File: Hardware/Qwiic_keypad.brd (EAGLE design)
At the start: 31.8 x 25.4 mm, 25 parts, among them J2 SMD, J3 PTH, J4 SMD, J6 AVR_SPI_PROG_3X2TESTPOINTS, U3 ATTINY84

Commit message: second layout complete
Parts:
- moved R3 6.48 mm to (14.0, 6.35)
- moved C4 5.24 mm to (7.62, 6.35)
- moved JP3 2.84 mm to (3.81, 1.27)
- moved JP5 1.27 mm to (17.8, 6.35)
- moved R1 1.27 mm to (24.1, 6.35)
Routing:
- net 3.3V: track 0.00 -> 77.5 mm, vias 0 -> 8
- net SDA: track 0.00 -> 70.1 mm, vias 0 -> 3
- net SCL: track 0.00 -> 52.8 mm, vias 0 -> 2
- net !RST: track 0.00 -> 31.2 mm, vias 0 -> 3
- net 7: track 0.00 -> 28.5 mm, vias 0 -> 1
- net MISO/6: track 0.00 -> 20.3 mm, vias 0 -> 1
- net 5: track 0.00 -> 18.1 mm, vias 0 -> 1
- net 2: track 0.00 -> 14.0 mm, vias 0 -> 1
- net GND: track 0.00 -> 12.9 mm, vias 0 -> 5
- net 1: track 0.00 -> 12.4 mm
- net 3: track 0.00 -> 10.4 mm, vias 0 -> 1
- net !INT: track 0.00 -> 9.16 mm
- net 4: track 0.00 -> 9.16 mm, vias 0 -> 1
- net ADD1: track 0.00 -> 6.92 mm
- net N$1: track 0.00 -> 5.09 mm
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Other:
- board text removed: "+"

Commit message: changed header from 7 pin to 9 pin to accomidate extra pin on the keypad itself
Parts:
- removed J9: (no value), SparkFun-Connectors:1X07_NO_SILK
- added J7: (no value), SparkFun-Connectors:1X09_NO_SILK
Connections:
- net 1: now also J7.2; no longer J9.1
- net 2: now also J7.3; no longer J9.2
- net 3: now also J7.4; no longer J9.3
- net 4: now also J7.5; no longer J9.4
- net 5: now also J7.6; no longer J9.5
- net 7: now also J7.8; no longer J9.7
- net MISO/6: now also J7.7; no longer J9.6
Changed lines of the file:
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@@
 <element name="JP1" library="SparkFun" package="MICRO-FIDUCIAL" value="FIDUCIALUFIDUCIAL" x="30.48" y="24.13" rot="MR0"/>
 <element name="JP3" library="SparkFun" package="MICRO-FIDUCIAL" value="FIDUCIALUFIDUCIAL" x="3.81" y="1.27" rot="MR0"/>
-<element name="J9" library="SparkFun-Connectors" package="1X07_NO_SILK" value="" x="8.89" y="24.13"/>
 <element name="J5" library="SparkFun-Connectors" package="1X01_NO_SILK" value="" x="22.86" y="1.27"/>
+<element name="J7" library="SparkFun-Connectors" package="1X09_NO_SILK" value="" x="6.35" y="24.13"/>
 </elements>
 <signals>
@@
 <signal name="4">
 <contactref element="U3" pad="10"/>
-<contactref element="J9" pad="4"/>
 <wire x1="17.78" y1="15.5" x2="17.78" y2="16.51" width="0.254" layer="1"/>
 <wire x1="17.78" y1="16.51" x2="17.272" y2="17.018" width="0.254" layer="1"/>
@@
 <wire x1="17.272" y1="17.018" x2="17.272" y2="20.828" width="0.254" layer="16"/>
 <wire x1="17.272" y1="20.828" x2="16.51" y2="21.59" width="0.254" layer="16"/>
-<wire x1="16.51" y1="21.59" x2="16.51" y2="24.13" width="0.254" layer="16"/>
+<contactref element="J7" pad="5"/>
+<wire x1="16.51" y1="24.13" x2="16.51" y2="21.59" width="0.254" layer="16"/>
 </signal>
 <signal name="3">
 <contactref element="U3" pad="11"/>
-<contactref element="J9" pad="3"/>
 <wire x1="16.51" y1="15.5" x2="16.51" y2="16.383" width="0.254" layer="1"/>
 <wire x1="16.51" y1="16.383" x2="16.383" y2="16.51" width="0.254" layer="1"/>
@@
 <wire x1="14.732" y1="17.018" x2="14.732" y2="20.828" width="0.254" layer="16"/>
 <wire x1="14.732" y1="20.828" x2="13.97" y2="21.59" width="0.254" layer="16"/>
-<wire x1="13.97" y1="21.59" x2="13.97" y2="24.13" width="0.254" layer="16"/>
+<contactref element="J7" pad="4"/>
+<wire x1="13.97" y1="24.13" x2="13.97" y2="21.59" width="0.254" layer="16"/>
 </signal>
 <signal name="2">
 <contactref element="U3" pad="12"/>
-<contactref element="J9" pad="2"/>
 <wire x1="15.24" y1="15.5" x2="15.24" y2="13.97" width="0.254" layer="1"/>
 <via x="15.24" y="13.97" extent="1-16" drill="0.381"/>
 <wire x1="15.24" y1="13.97" x2="13.97" y2="13.97" width="0.254" layer="16"/>
 <wire x1="13.97" y1="13.97" x2="11.43" y2="16.51" width="0.254" layer="16"/>
-<wire x1="11.43" y1="16.51" x2="11.43" y2="24.13" width="0.254" layer="16"/>
+<contactref element="J7" pad="3"/>
+<wire x1="11.43" y1="24.13" x2="11.43" y2="16.51" width="0.254" layer="16"/>
 </signal>
 <signal name="1">
 <contactref element="U3" pad="13"/>
-<contactref element="J9" pad="1"/>
 <wire x1="13.97" y1="15.5" x2="13.97" y2="16.51" width="0.254" layer="1"/>
 <wire x1="13.97" y1="16.51" x2="13.843" y2="16.637" width="0.254" layer="1"/>
 <wire x1="13.843" y1="16.637" x2="10.922" y2="16.637" width="0.254" layer="1"/>
 <wire x1="10.922" y1="16.637" x2="8.89" y2="18.669" width="0.254" layer="1"/>
-<wire x1="8.89" y1="24.13" x2="8.89" y2="18.669" width="0.254" layer="1"/>
+<contactref element="J7" pad="2"/>
+<wire x1="8.89" y1="18.669" x2="8.89" y2="24.13" width="0.254" layer="1"/>
 </signal>
 <signal name="!RST">
@@
 <contactref element="U3" pad="8"/>
 <contactref element="J6" pad="1"/>
-<contactref element="J9" pad="6"/>
 <wire x1="13.97" y1="18.669" x2="19.304" y2="18.669" width="0.254" layer="1"/>
-<wire x1="21.59" y1="24.13" x2="21.59" y2="15.24" width="0.254" layer="16"/>
 <wire x1="20.32" y1="15.5" x2="21.33" y2="15.5" width="0.254" layer="1"/>
 <wire x1="21.33" y1="15.5" x2="21.59" y2="15.24" width="0.254" layer="1"/>
@@
 <wire x1="13.335" y1="17.78" x2="13.335" y2="18.034" width="0.254" layer="1"/>
 <wire x1="13.335" y1="18.034" x2="13.97" y2="18.669" width="0.254" layer="1"/>
+<contactref element="J7" pad="7"/>
+<wire x1="21.59" y1="24.13" x2="21.59" y2="15.24" width="0.254" layer="16"/>
 </signal>
 <signal name="7">
 <contactref element="U3" pad="2"/>
-<contactref element="J9" pad="7"/>
-<wire x1="24.13" y1="24.13" x2="24.13" y2="8.89" width="0.254" layer="16"/>
 <wire x1="13.97" y1="9.9" x2="13.97" y2="8.509" width="0.254" layer="1"/>
 <via x="13.97" y="8.509" extent="1-16" drill="0.381"/>
@@
 <wire x1="13.97" y1="8.128" x2="15.24" y2="6.858" width="0.254" layer="16"/>
 <wire x1="22.098" y1="6.858" x2="24.13" y2="8.89" width="0.254" layer="16"/>
+<contactref element="J7" pad="8"/>
+<wire x1="24.13" y1="24.13" x2="24.13" y2="8.89" width="0.254" layer="16"/>
 </signal>
 <signal name="5">
 <contactref element="U3" pad="5"/>
-<contactref element="J9" pad="5"/>
 <wire x1="17.78" y1="9.9" x2="17.78" y2="8.763" width="0.254" layer="1"/>
 <via x="17.78" y="8.763" extent="1-16" drill="0.381"/>
@@
 <wire x1="20.32" y1="16.51" x2="20.32" y2="21.59" width="0.254" layer="16"/>
 <wire x1="20.32" y1="21.59" x2="19.05" y2="22.86" width="0.254" layer="16"/>
-<wire x1="19.05" y1="22.86" x2="19.05" y2="24.13" width="0.254" layer="16"/>
+<contactref element="J7" pad="6"/>
+<wire x1="19.05" y1="24.13" x2="19.05" y2="22.86" width="0.254" layer="16"/>
 </signal>
 <signal name="SCL">

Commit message: Adding production ready firmware. Adding examples.
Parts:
- J2, J4: value SMD -> (none); device SparkX:1X04_1MM_RA -> SparkFun-Connectors:1X04_1MM_RA
- J7: value (none) -> Keypad
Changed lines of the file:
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@@
 <layer number="59" name="tCarbon" color="7" fill="1" visible="no" active="no"/>
 <layer number="60" name="bCarbon" color="7" fill="1" visible="no" active="no"/>
+<layer number="88" name="SimResults" color="9" fill="1" visible="no" active="yes"/>
+<layer number="89" name="SimProbes" color="9" fill="1" visible="no" active="yes"/>
 <layer number="90" name="Modules" color="5" fill="1" visible="no" active="no"/>
 <layer number="91" name="Nets" color="2" fill="1" visible="no" active="no"/>
@@
 <element name="JP2" library="SparkFun" package="MICRO-FIDUCIAL" value="FIDUCIALUFIDUCIAL" x="30.861" y="0.889"/>
 <element name="JP6" library="SparkFun" package="MICRO-FIDUCIAL" value="FIDUCIALUFIDUCIAL" x="0.762" y="24.638"/>
-<element name="J2" library="SparkX" package="1X04_1MM_RA" value="SMD" x="5.08" y="12.7" rot="R270"/>
+<element name="J2" library="SparkFun-Connectors" package="1X04_1MM_RA" value="" x="5.08" y="12.7" rot="R270">
+<attribute name="PROD_ID" value="CONN-13694" x="5.08" y="12.7" size="1.778" layer="27" rot="R270" display="off"/>
+<attribute name="VALUE" value="" x="5.08" y="12.7" size="1.778" layer="27" rot="R270" display="off"/>
+</element>
 <element name="J3" library="SparkX" package="1X04_NO_SILK" value="PTH" x="10.16" y="1.27" smashed="yes">
 <attribute name="VALUE" x="8.89" y="-0.762" size="0.6096" layer="27" font="vector" ratio="20"/>
@@
 <attribute name="PROD_ID" value="CAP-00810" x="7.62" y="6.35" size="1.778" layer="27" font="vector" ratio="15" rot="R180" display="off"/>
 </element>
-<element name="J4" library="SparkX" package="1X04_1MM_RA" value="SMD" x="26.67" y="12.7" rot="R90"/>
+<element name="J4" library="SparkFun-Connectors" package="1X04_1MM_RA" value="" x="26.67" y="12.7" rot="R90">
+<attribute name="PROD_ID" value="CONN-13694" x="26.67" y="12.7" size="1.778" layer="27" rot="R90" display="off"/>
+<attribute name="VALUE" value="" x="26.67" y="12.7" size="1.778" layer="27" rot="R90" display="off"/>
+</element>
 <element name="LOGO1" library="SparkFun-Aesthetics" package="OSHW-LOGO-MINI" value="OSHW-LOGOMINI" x="2.54" y="21.59" rot="MR0"/>
 <element name="U$1" library="SparkX" package="SPARKX-SMALL" value="SPARKX-LOGO3" x="30.48" y="12.7" rot="MR90"/>
@@
 <element name="J1" library="SparkFun-Connectors" package="1X01_NO_SILK" value="" x="20.32" y="1.27"/>
 <element name="R3" library="SparkFun-Resistors" package="0603" value="10k" x="13.97" y="6.35">
-<attribute name="PROD_ID" value="RES-08272" x="13.97" y="6.35" size="1.778" layer="27" font="vector" ratio="15" display="off"/>
+<attribute name="PROD_ID" value="RES-00824" x="13.97" y="6.35" size="1.778" layer="27" font="vector" ratio="15" display="off"/>
 </element>
 <element name="JP5" library="SparkFun-Jumpers" package="SMT-JUMPER_2_NC_PASTE_NO-SILK" value="JUMPER-SMT_2_NC_PASTE_NO-SILK" x="17.78" y="6.35" smashed="yes">
@@
 </element>
 <element name="R1" library="SparkFun-Resistors" package="0603" value="4.7k" x="24.13" y="6.35">
-<attribute name="PROD_ID" value="RES-08272" x="24.13" y="6.35" size="1.778" layer="27" font="vector" ratio="15" display="off"/>
+<attribute name="PROD_ID" value="RES-07857" x="24.13" y="6.35" size="1.778" layer="27" font="vector" ratio="15" display="off"/>
 </element>
 <element name="J6" library="SparkFun-Connectors" package="2X3_TEST_POINTS" value="AVR_SPI_PROG_3X2TESTPOINTS" x="15.875" y="19.05"/>
@@
 </element>
 <element name="R6" library="SparkFun-Resistors" package="0603" value="1k" x="1.27" y="19.05" rot="R270">
-<attribute name="PROD_ID" value="RES-08272" x="1.27" y="19.05" size="1.778" layer="27" font="vector" ratio="15" rot="R270" display="off"/>
+<attribute name="PROD_ID" value="RES-07856" x="1.27" y="19.05" size="1.778" layer="27" font="vector" ratio="15" rot="R270" display="off"/>
 </element>
 <element name="JP1" library="SparkFun" package="MICRO-FIDUCIAL" value="FIDUCIALUFIDUCIAL" x="30.48" y="24.13" rot="MR0"/>
 <element name="JP3" library="SparkFun" package="MICRO-FIDUCIAL" value="FIDUCIALUFIDUCIAL" x="3.81" y="1.27" rot="MR0"/>
 <element name="J5" library="SparkFun-Connectors" package="1X01_NO_SILK" value="" x="22.86" y="1.27"/>
-<element name="J7" library="SparkFun-Connectors" package="1X09_NO_SILK" value="" x="6.35" y="24.13"/>
+<element name="J7" library="SparkFun-Connectors" package="1X09_NO_SILK" value="Keypad" x="6.35" y="24.13"/>
 </elements>
 <signals>

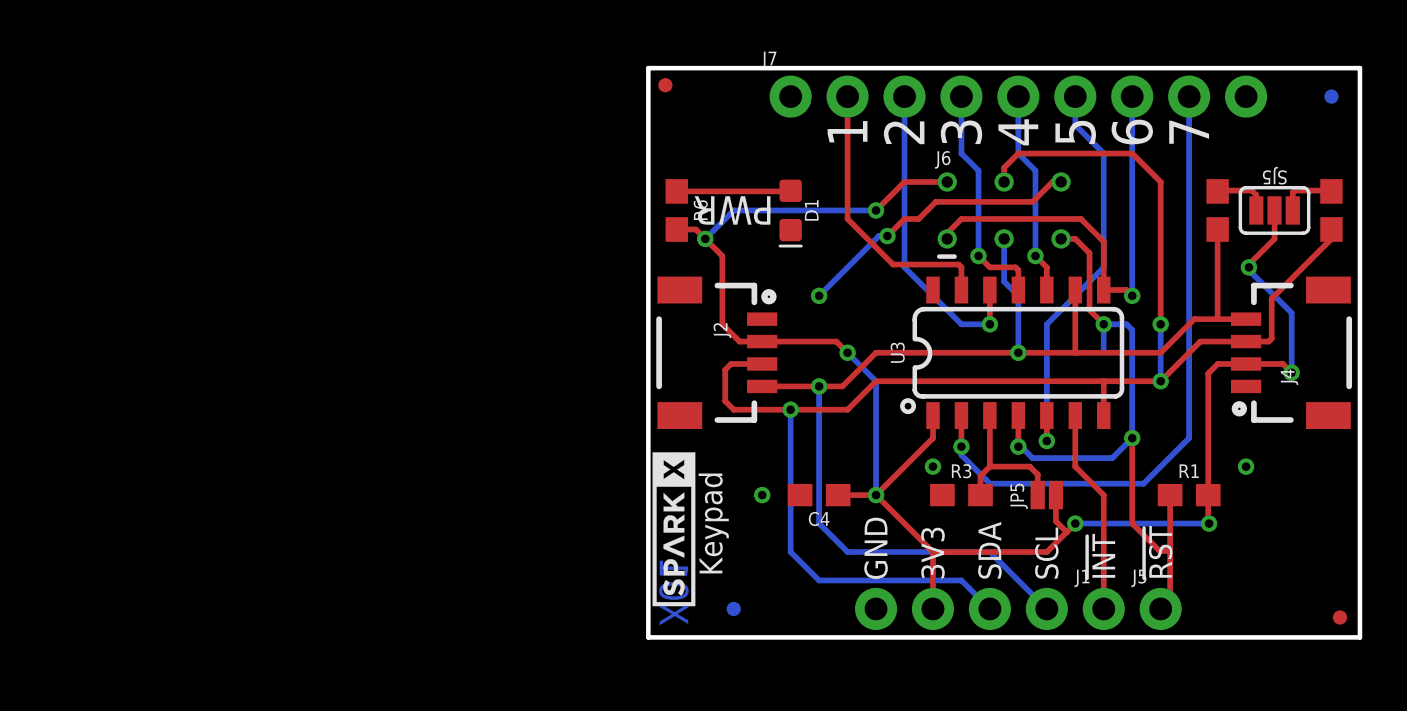
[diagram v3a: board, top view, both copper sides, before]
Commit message: Smaller board size.
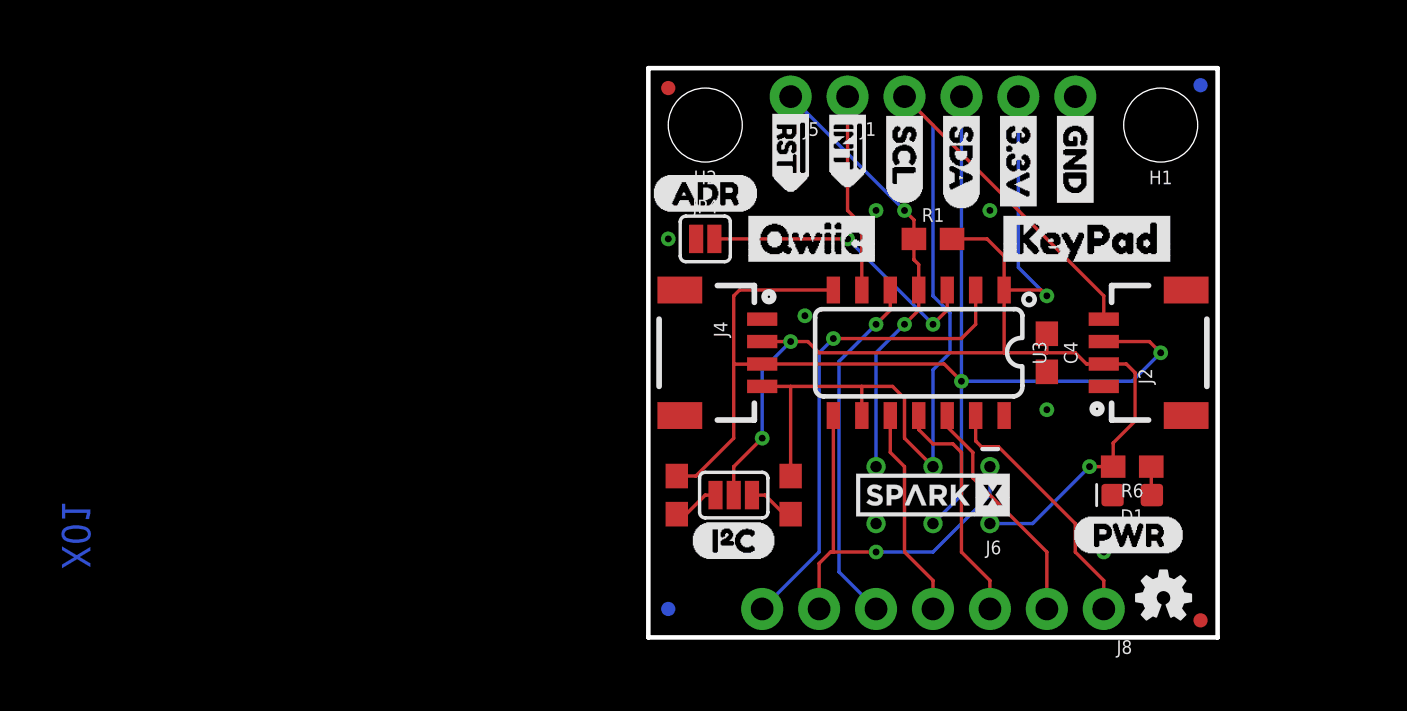
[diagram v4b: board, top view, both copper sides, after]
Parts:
- removed J7: Keypad, SparkFun-Connectors:1X09_NO_SILK
- removed JP5: JUMPER-SMT_2_NC_PASTE_NO-SILK, SparkFun-Jumpers:SMT-JUMPER_2_NC_PASTE_NO-SILK
- removed R3: 10k, SparkFun-Resistors:0603
- added H1, H2: STAND-OFF, SparkFun-Hardware:STAND-OFF
- added J8: (no value), SparkFun-Connectors:1X07_NO_SILK
- added JP4: (no value), SparkFun-Jumpers:SMT-JUMPER_2_NO_SILK
- added U$10: (no value), Labels-0_04:(ADR)
- added U$11: (no value), Labels-0_04:#RST>
- added U$12: (no value), buzzard_labels (18):QWIIC2
- added U$13: (no value), buzzard_labels (18):KEYPAD3
- added U$3: (no value), Labels-0_04:3.3V
- added U$4: (no value), Labels-0_04:GND
- added U$5: (no value), Labels-0_04:SDA
- added U$6: (no value), Labels-0_04:SCL
- added U$7: (no value), Labels-0_04:#INT>
- added U$8: (no value), Labels-0_04:(PWR)
- added U$9: (no value), Labels-0_04:(I_SUPER2_C)
- moved FRAME1 38.2 mm to (-14.0, -11.4)
- moved JP2 38.2 mm to (0.89, 24.5), turned to 180 degrees
- moved JP1 37.4 mm to (0.89, 1.27), turned to 180 degrees
- moved JP6 33.8 mm to (24.6, 0.76), turned to 180 degrees
- moved R4 31.9 mm to (1.27, 6.35), turned to 270 degrees
- moved JP3 31.3 mm to (24.6, 24.6), turned to 180 degrees
- moved U$1 29.2 mm to (1.27, 12.7), turned to 270 degrees
- moved LOGO1 28.5 mm to (23.0, 1.78), flipped to the top
- moved J5 28.2 mm to (6.35, 24.1), turned to 180 degrees
- moved SJ5 27.3 mm to (3.81, 6.35), turned to 180 degrees
- moved J1 25.6 mm to (8.89, 24.1), turned to 180 degrees
- moved J3 24.5 mm to (19.1, 24.1), turned to 180 degrees
- moved R6 23.3 mm to (21.6, 7.62), turned to 180 degrees
- moved R2 22.9 mm to (6.35, 6.35), turned to 270 degrees
- moved J4 21.6 mm to (5.08, 12.7), turned to 270 degrees
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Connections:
- net 1: now also J8.1; no longer J7.2
- net 2: now also J8.2; no longer J7.3
- net 3: now also J8.3; no longer J7.4
- net 3.3V: no longer JP5.2
- net 4: now also J8.4; no longer J7.5
- net 5: now also J8.5; no longer J7.6
- net 7: now also J8.7; no longer J7.8
- net ADD1: now also JP4.2; no longer JP5.1, R3.2
- net GND: now also JP4.1; no longer R3.1
- net MISO/6: now also J8.6; no longer J7.7
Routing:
- net 3.3V: track 77.5 -> 55.5 mm, vias 8 -> 4
- net SDA: track 70.1 -> 56.4 mm, vias 3 -> 2
- net GND: track 12.9 -> 0.00 mm, vias 5 -> 6
- net !RST: track 31.2 -> 19.7 mm, vias 3 -> 2
- net 7: track 28.5 -> 21.5 mm
- net ADD1: track 6.92 -> 13.1 mm, vias 0 -> 2
- net SCL: track 52.8 -> 46.7 mm, vias 2 -> 0
- net N$1: track 5.09 -> 1.28 mm
- net 2: track 14.0 -> 10.5 mm, vias 1 -> 0
- net 5: track 18.1 -> 15.9 mm
- net MISO/6: track 20.3 -> 18.3 mm
- net 1: track 12.4 -> 11.4 mm
- net SDA_PU1: track 2.59 -> 2.08 mm
- net 4: track 9.16 -> 9.42 mm, vias 1 -> 0
- net 3: track 10.4 -> 10.5 mm, vias 1 -> 0
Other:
- board size 31.8 x 25.4 mm -> 25.4 x 25.4 mm
- board text removed: "!INT"
- board text removed: "!RST"
- board text removed: "!RST\"
- board text removed: "1"
- board text removed: "2"
- board text removed: "3"
- board text removed: "3V3"
- board text removed: "4"
- board text removed: "5"
- board text removed: "6"
- board text removed: "7"
- board text removed: "GND"
- board text removed: "Keypad"
- board text removed: "PWR"
- board text removed: "Qwiic Keypad"
- board text removed: "SCL"
- board text removed: "SDA"
